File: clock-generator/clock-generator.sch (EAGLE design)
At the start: 61 parts, among them IC1 24C00TS, U1 SN74LVC1G04DBV, U3 ATSAMD11-QFN24, U4 SI5351C, U5 IP4234CZ6, U6 IP4234CZ6, X1 MINI-USB-SHIELD-UX60A-MB-5ST, X2 JACK2.5_SJ-2523, X4 1-227161-0

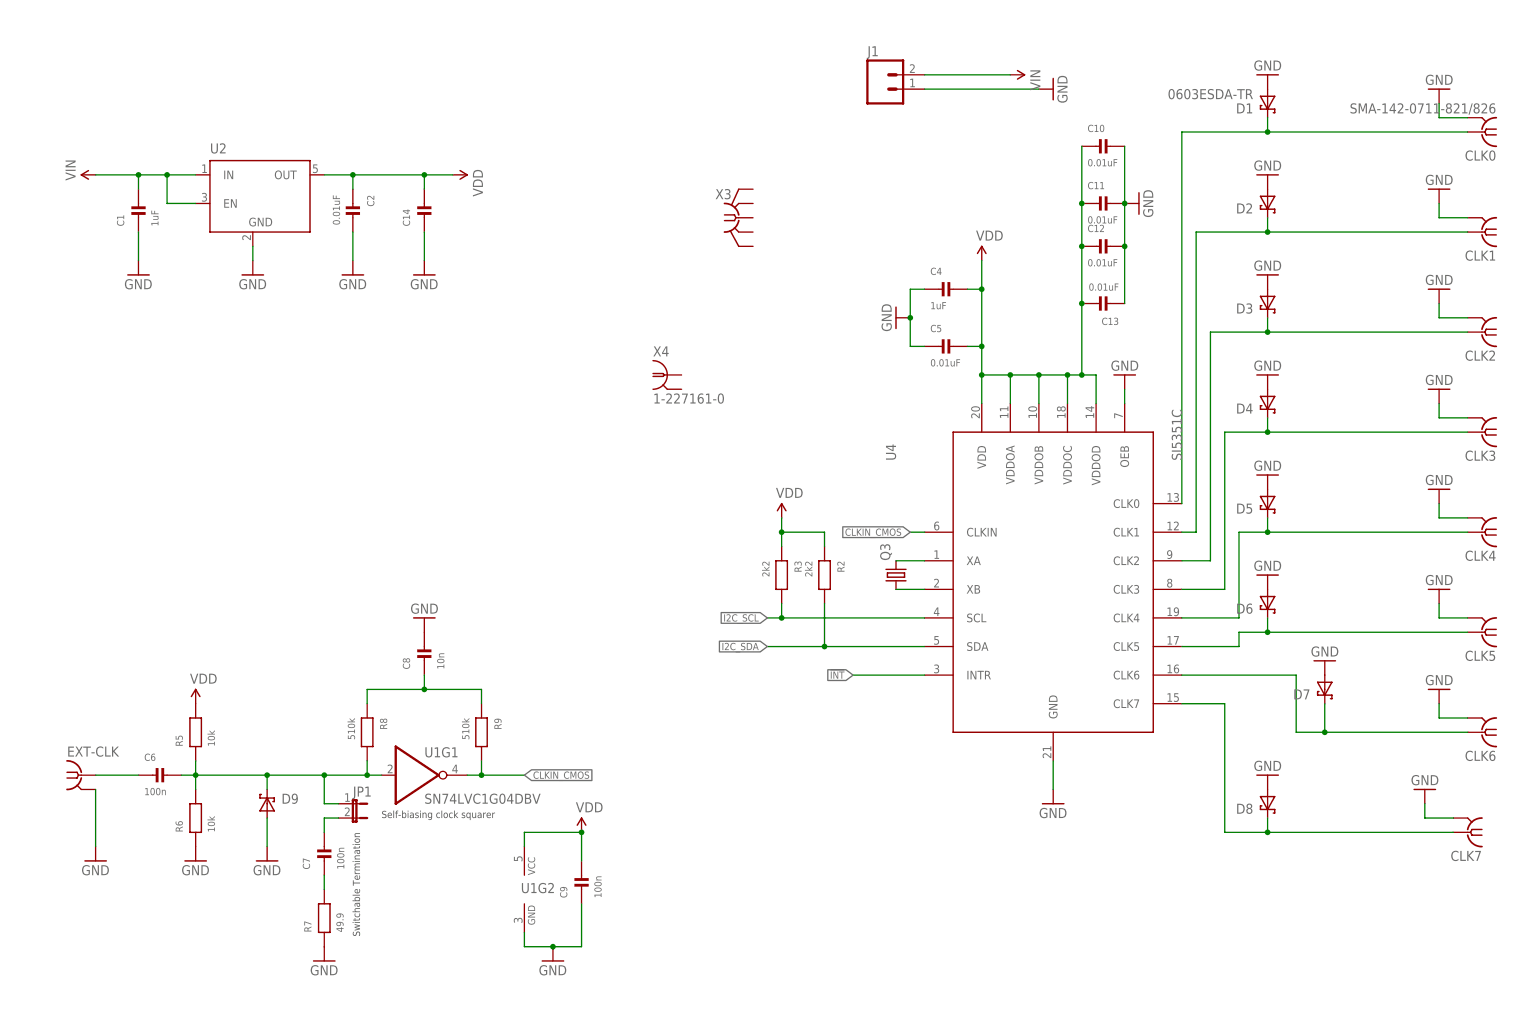
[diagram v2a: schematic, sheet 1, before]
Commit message: clock-generator: Most of the layout
Traces are intended for dual-layer 1mm FR4 PCB with 35um copper.
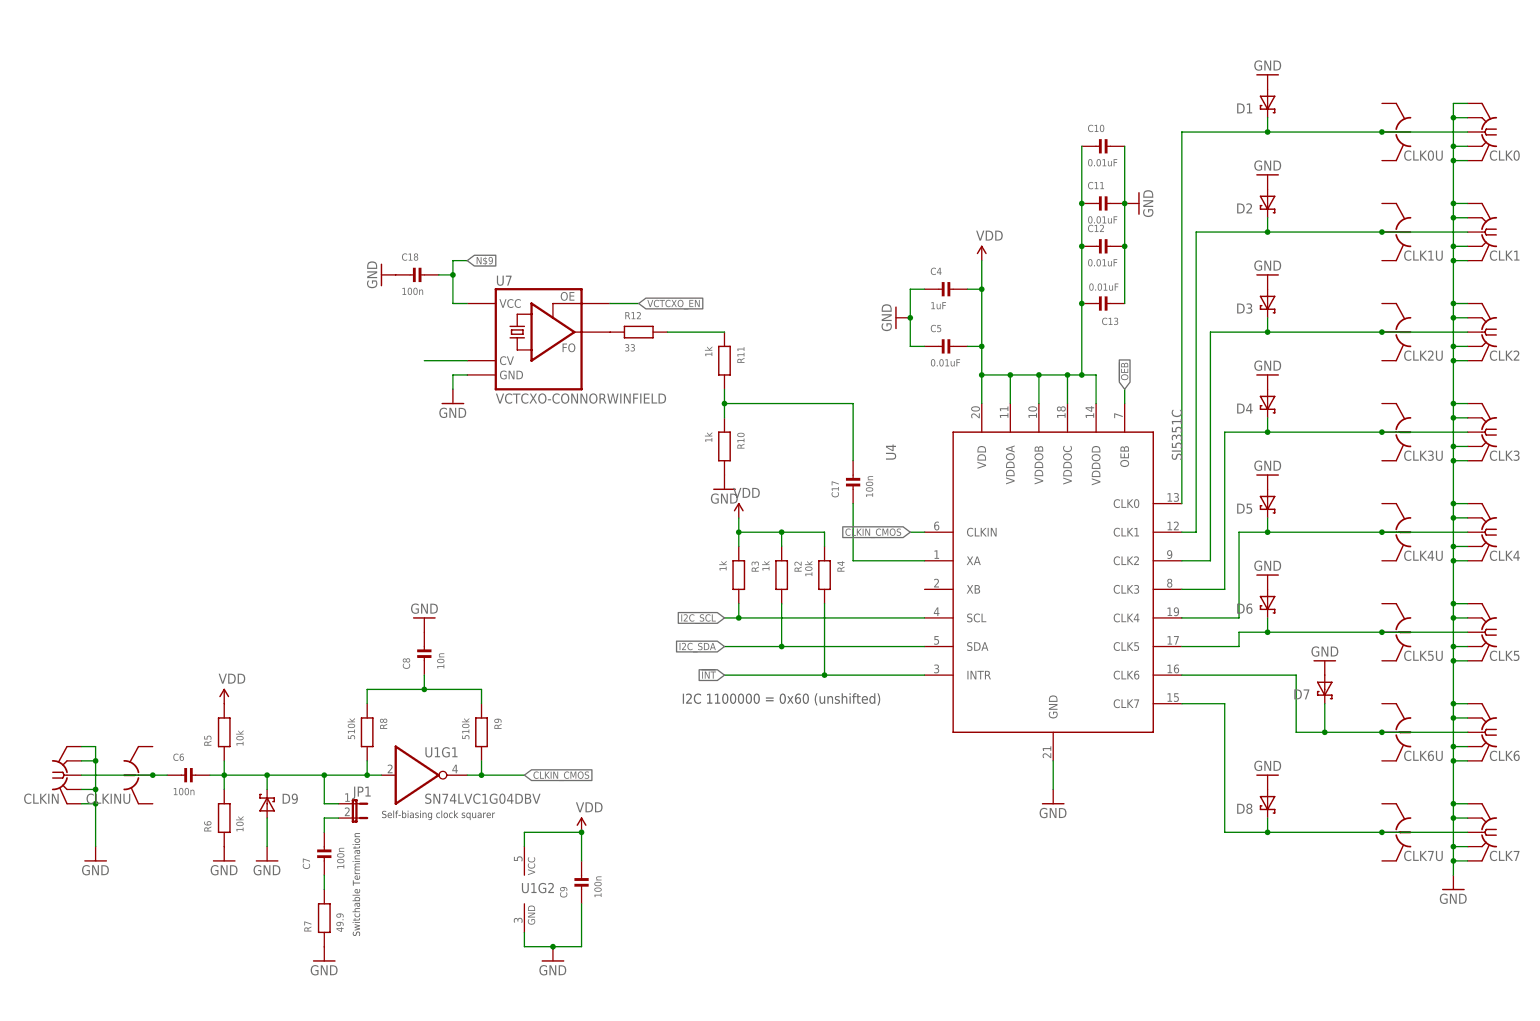
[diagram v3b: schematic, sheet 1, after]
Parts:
- removed EXT-CLK: SMA-142-0711-821/826, con-coax:SMA-142-0711-821/826
- removed J1: (no value), SparkFun-Connectors:M02LOCK_LONGPADS
- removed L701: 744231091, Wuerth_Elektronik_eiSos_V6_20140807:WE-CNSW_0805
- removed Q3: (no value), jackens:CRYSTAL-SMD
- removed X4: 1-227161-0, con-coax:1-227161-0
- added C17, C18: 100n, rc-sysmocom:CAP_CERAMIC_0603
- added CLK0U, CLK1U, CLK2U, CLK3U, CLK4U, CLK5U, CLK6U, CLK7U, CLKINU: (no value), laforge:HRS_UFL
- added CLKIN: (no value), laforge:SMA-F-S-TH
- added D10: DIODDE-ZENER-SMA, diodes-sysmocom:DIODDE-ZENER-SMA
- added F1: (no value), littlefuse:POLYFUSE-1206L
- added K2: 694108106102, Wurth_Elektronik_Electromechanic_DC_Power_Jack_Connectors_rev15c:694108106102
- added L1: 744231091, Wuerth_Elektronik_eiSos_V6_20140807:WE-CNSW_0805
- added L2: (no value), rc-sysmocom:INDUCTOR_0805
- added LED1: green, LED-PLCC2:LEDPLCC2-MIN
- added LED2: yellow, LED-PLCC2:LEDPLCC2-MIN
- added M1: MENTOR_12701001, Mentor_lightpipe:MENTOR_12701001
- added R10, R11: 1k, rc-sysmocom:RESISTOR_0603
- added R12: 33, rc-sysmocom:RESISTOR_0603
- added R13, R14: 330, rc-sysmocom:RESISTOR_0603
- added R4: 10k, rc-sysmocom:RESISTOR_0603
- added U7: VCTCXO-CONNORWINFIELD, Connor-Winfield_VCTCXO:VCTCXO-CONNORWINFIELD
- C1, C2, C6, C7, C9: device rc-sysmocom:CAP_CERAMIC0603 -> rc-sysmocom:CAP_CERAMIC_0603
- C16, C701: device rc-sysmocom:CAP_CERAMIC_0402 -> rc-sysmocom:CAP_CERAMIC_0603
- CLK0, CLK1, CLK2, CLK3, CLK4, CLK5, CLK6, CLK7: value SMA-142-0711-821/826 -> (none); device con-coax:SMA-142-0711-821/826 -> laforge:SMA-F-S-TH
- R2, R3: value 2k2 -> 1k
- X3: device laforge:SMA-F-S-TH -> laforge:PINHD-1X3LOCK_NO_SILK
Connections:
- removed net N$22: L701.2, U5.2B
- removed net N$43: L701.3, U5.1B
- removed net VIN: C1.2, J1.2, U2.EN, U2.IN
- removed net XB: Q3.1, U4.XB
- new net !LED_YELLOW: LED2.C
- new net !OEB: U3.PA17/X5/Y11/SC1P3/SC2P3/TC1WO1/TCC0WO7/GCLK_IO3, U4.OEB
- new net N$1: R11.1, R12.2
- new net N$10: U7.CV
- new net N$11: LED1.A, R13.1
- new net N$12: LED2.A, R14.1
- new net N$13: C15.2, C3.2, L2.1, U3.VDD
- new net N$14: C1.2, D10.C, F1.1, U2.EN, U2.IN
- new net N$15: F1.2, K2.1
- new net N$2: C17.2, R10.1, R11.2
- new net N$4: R12.1, U7.FO
- new net N$9: C18.2, U7.VCC
- new net USB1_D_N: L1.3, U5.2B
- new net USB1_D_P: L1.2, U5.1B
- new net VCTCXO_EN: U7.OE
- net !INT: now also R4.2
- net CLK0_LINE: now also CLK0U.1
- net CLK1_LINE: now also CLK1U.1
- net CLK2_LINE: now also CLK2U.1
- net CLK3_LINE: now also CLK3U.1
- net CLK4_LINE: now also CLK4U.1
- net CLK5_LINE: now also CLK5U.1
- net CLK6_LINE: now also CLK6U.1
- net CLK7_LINE: now also CLK7U.1
- net CLKIN: now also CLKIN.1, CLKINU.1; no longer EXT-CLK.1
- net GND: now also C18.1, CLK0.GND@1, CLK0.GND@2, CLK0.GND@3, CLK0.GND@4, CLK1.GND@1, CLK1.GND@2, CLK1.GND@3, CLK1.GND@4, CLK2.GND@1, CLK2.GND@2, CLK2.GND@3, CLK2.GND@4, CLK3.GND@1, CLK3.GND@2, CLK3.GND@3, CLK3.GND@4, CLK4.GND@1, CLK4.GND@2, CLK4.GND@3, CLK4.GND@4, CLK5.GND@1, CLK5.GND@2, CLK5.GND@3, CLK5.GND@4, CLK6.GND@1, CLK6.GND@2, CLK6.GND@3, CLK6.GND@4, CLK7.GND@1, CLK7.GND@2, CLK7.GND@3, CLK7.GND@4, CLKIN.GND@1, CLKIN.GND@2, CLKIN.GND@3, CLKIN.GND@4, D10.A, IC1.A0, IC1.A1, IC1.A2, K2.2, K2.3, LED1.C, R10.2, U7.GND, X3.1; no longer CLK0.2, CLK1.2, CLK2.2, CLK3.2, CLK4.2, CLK5.2, CLK6.2, CLK7.2, EXT-CLK.2, J1.1, U4.OEB
- net N$6: now also X3.3
- net N$8: now also X3.2
- net USB_D_N: now also L1.4; no longer L701.1
- net USB_D_P: now also L1.1; no longer L701.4
- net VDD: now also L2.2, R13.2, R14.2, R4.1; no longer C15.2, C3.2, U3.VDD
- net XA: now also C17.1; no longer Q3.2
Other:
- note added: "I2C 1100000 = 0x60 (unshifted)"
- moved on the sheet: C6, R1, R2, R3, R5, R6, U6

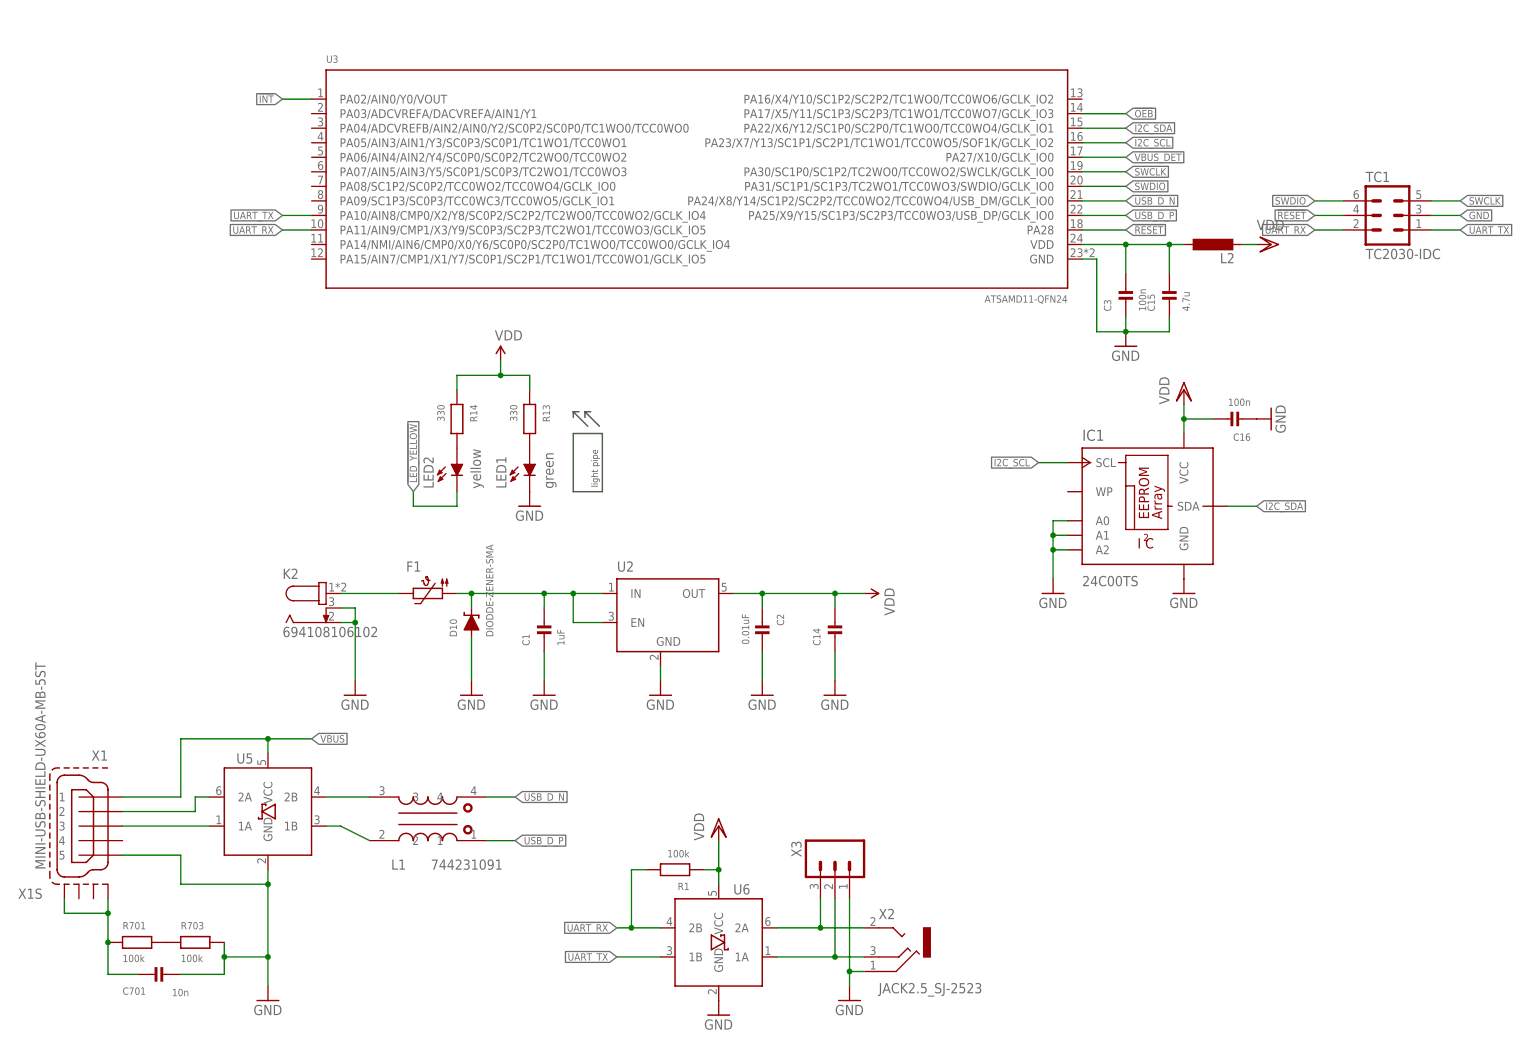
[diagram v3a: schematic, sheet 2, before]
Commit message: clock-gen: Add SPI; UEXT header; mounting holes; do layout/routing
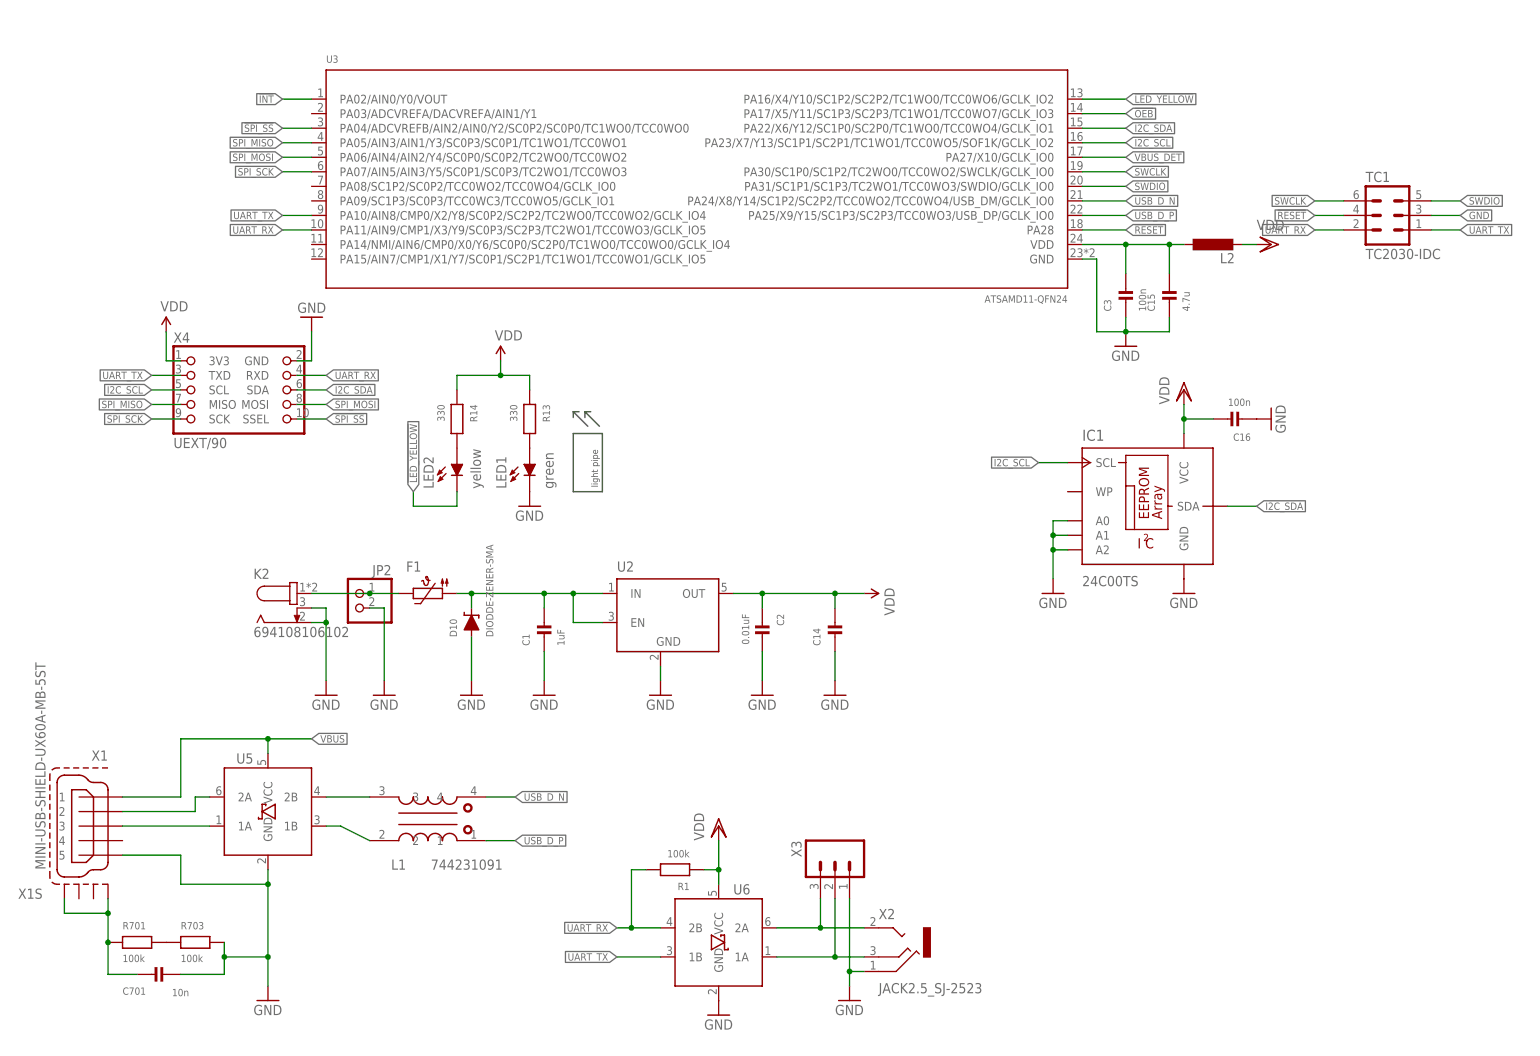
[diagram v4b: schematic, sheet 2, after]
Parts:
- added JP2: (no value), laforge:PINHD-1X2
- added X4: UEXT/90, laforge:UEXT/90
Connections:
- new net !SPI_SS: U3.PA04/ADCVREFB/AIN2/AIN0/Y2/SC0P2/SC0P0/TC1WO0/TCC0WO0, X4.SSEL
- new net SPI_MISO: U3.PA05/AIN3/AIN1/Y3/SC0P3/SC0P1/TC1WO1/TCC0WO1, X4.MISO
- new net SPI_MOSI: U3.PA06/AIN4/AIN2/Y4/SC0P0/SC0P2/TC2WO0/TCC0WO2, X4.MOSI
- new net SPI_SCK: U3.PA07/AIN5/AIN3/Y5/SC0P1/SC0P3/TC2WO1/TCC0WO3, X4.SCK
- net !LED_YELLOW: now also U3.PA16/X4/Y10/SC1P2/SC2P2/TC1WO0/TCC0WO6/GCLK_IO2
- net GND: now also JP2.2, X4.GND
- net I2C_SCL: now also X4.SCL
- net I2C_SDA: now also X4.SDA
- net N$15: now also JP2.1
- net SWCLK: now also TC1.6; no longer TC1.5
- net SWDIO: now also TC1.5; no longer TC1.6
- net UART_RX: now also X4.RXD
- net UART_TX: now also X4.TXD
- net VDD: now also X4.3V3
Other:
- moved on the sheet: K2

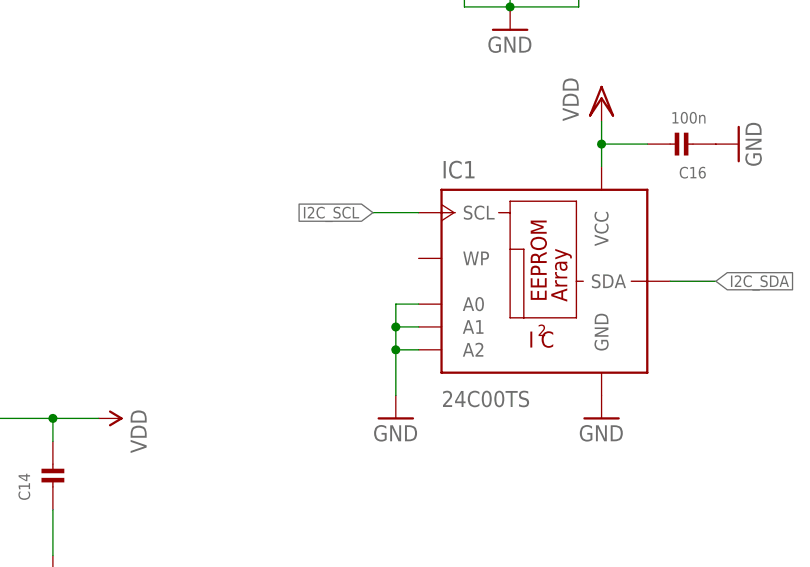
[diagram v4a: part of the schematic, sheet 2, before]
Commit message: clock-gen: Connect EEPROM WP to GND to disable write-protect
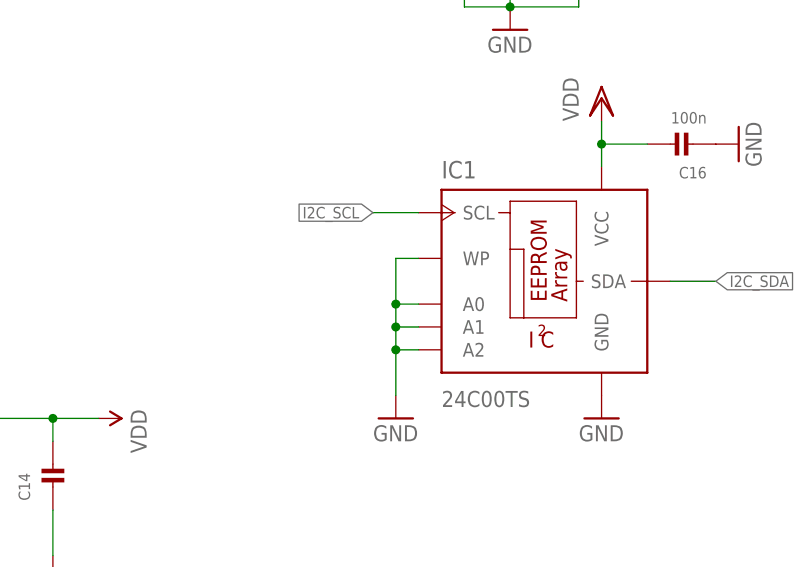
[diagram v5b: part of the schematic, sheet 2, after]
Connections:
- net GND: now also IC1.WP
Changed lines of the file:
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@@
 <junction x="180.34" y="88.9"/>
 <pinref part="GND7" gate="1" pin="GND"/>
+<pinref part="IC1" gate="G$1" pin="WP"/>
+<wire x1="182.88" y1="96.52" x2="180.34" y2="96.52" width="0.1524" layer="91"/>
+<wire x1="180.34" y1="96.52" x2="180.34" y2="91.44" width="0.1524" layer="91"/>
+<junction x="180.34" y="91.44"/>
 </segment>
 <segment>
